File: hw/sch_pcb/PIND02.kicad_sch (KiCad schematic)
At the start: 58 parts, among them J1 Conn_Coaxial, J2 MLAB I2C interface, J3 HEADER_2x01, M1 HOLE M3, M2 HOLE M3, M3 HOLE, M4 HOLE, M5 RFShield_TwoPieces, Q1 2SK2394-6, U1 OPA2314, U3 ISL21080DIH312Z-TK, U3 SHT31-DIS, U4 TPS613222ADBV

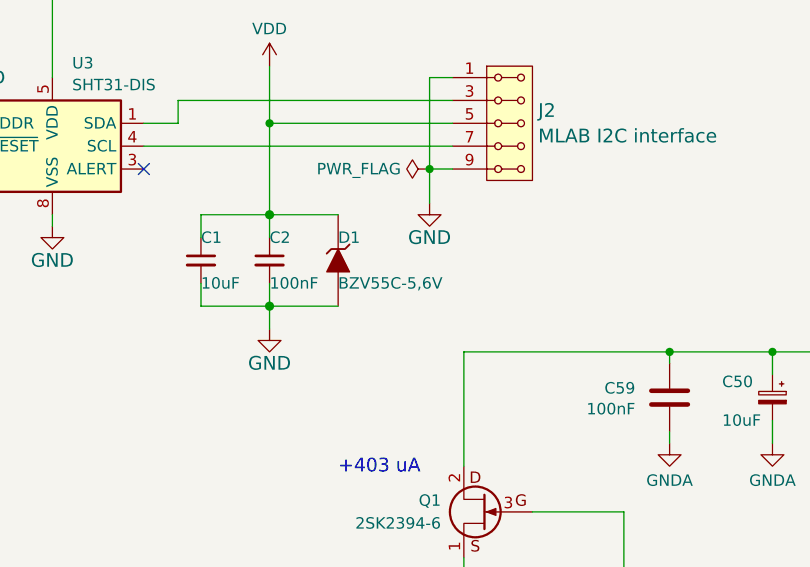
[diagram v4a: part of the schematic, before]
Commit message: Improve protection diode type and footprint.
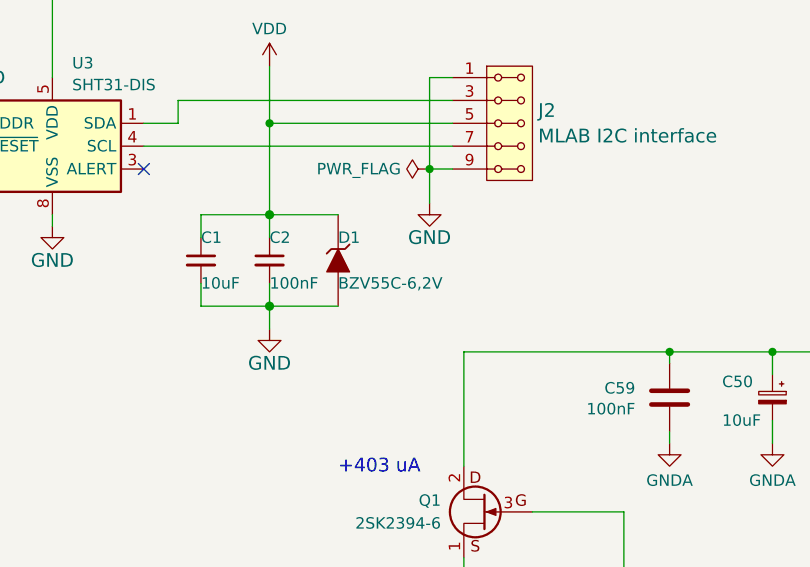
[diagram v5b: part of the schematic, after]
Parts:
- C2: UST_ID 5c70984812875079b91f8bf2 -> 5c70984712875079b91f8b4c; UST_id C0805_100n -> (none)
- D1: value BZV55C-5,6V -> BZV55C-6,2V; footprint Diode_SMD:D_SMA -> Diode_SMD:D_MiniMELF; UST_ID 5c70984512875079b91f88b2 -> 604b0326128750769e5b0f93
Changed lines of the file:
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@@
       (effects (font (size 1.524 1.524)))
     )
-    (property "UST_id" "C0805_100n" (at 66.04 54.61 0)
-      (effects (font (size 1.27 1.27)) hide)
-    )
-    (property "UST_ID" "5c70984812875079b91f8bf2" (at -184.15 83.82 0)
+    (property "UST_ID" "5c70984712875079b91f8b4c" (at -184.15 83.82 0)
       (effects (font (size 1.27 1.27)) hide)
     )
@@
       (effects (font (size 1.27 1.27)) (justify left))
     )
-    (property "Value" "BZV55C-5,6V" (at 73.66 57.15 90)
-      (effects (font (size 1.27 1.27)) (justify left))
-    )
-    (property "Footprint" "Diode_SMD:D_SMA" (at 73.66 54.61 0)
+    (property "Value" "BZV55C-6,2V" (at 73.66 57.15 90)
+      (effects (font (size 1.27 1.27)) (justify left))
+    )
+    (property "Footprint" "Diode_SMD:D_MiniMELF" (at 73.66 54.61 0)
       (effects (font (size 1.524 1.524)) hide)
     )
@@
       (effects (font (size 1.524 1.524)))
     )
-    (property "UST_ID" "5c70984512875079b91f88b2" (at 73.66 54.61 0)
-      (effects (font (size 1.27 1.27)) hide)
-    )
+    (property "UST_ID" "604b0326128750769e5b0f93" (at 73.66 54.61 0)
+      (effects (font (size 1.27 1.27)) hide)
+    )

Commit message: Edit UST_ID
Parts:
- U3: UST_ID (none) -> 5c70984612875079b91f89e4
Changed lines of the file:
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@@
       (effects (font (size 1.27 1.27)) hide)
     )
-    (property "UST_ID" "" (at 41.91 41.91 0)
+    (property "UST_ID" "5c70984612875079b91f89e4" (at 41.91 41.91 0)
       (effects (font (size 1.27 1.27)) hide)
     )

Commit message: Edit UST_ID
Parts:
- C15: UST_ID 6508354d462c6d9e7205425e -> 651abc26462c6d9e720551fa
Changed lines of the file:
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@@
       (effects (font (size 1.27 1.27)) hide)
     )
-    (property "UST_ID" "6508354d462c6d9e7205425e" (at 162.56 158.75 0)
+    (property "UST_ID" "651abc26462c6d9e720551fa" (at 162.56 158.75 0)
       (effects (font (size 1.27 1.27)) hide)
     )

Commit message: Increase gain.
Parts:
- R9: value 4k7 -> 10k; UST_ID 5c70984612875079b91f8995 -> (none)
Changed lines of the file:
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@@
       (effects (font (size 1.27 1.27)) (justify left))
     )
-    (property "Value" "4k7" (at 162.56 149.86 90)
+    (property "Value" "10k" (at 162.56 149.86 90)
       (effects (font (size 1.27 1.27)))
     )
@@
       (effects (font (size 1.27 1.27)) hide)
     )
-    (property "UST_ID" "5c70984612875079b91f8995" (at 162.56 149.86 0)
+    (property "UST_ID" "" (at 162.56 149.86 0)
       (effects (font (size 1.27 1.27)) hide)
     )
